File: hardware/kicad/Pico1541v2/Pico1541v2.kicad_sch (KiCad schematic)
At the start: 48 parts, among them J1 SWD, J2 Serial, J3 Display/Keys, J4 Micro SD Card, J5 OLED/Key_Hat, J6 OLED, J7 DIN-6, Q1 MMBT3904, SW1 Reset, SW2 Button1, SW3 Button2, SW4 Button3, SW5 Button4, U1 74LS06, U2 SRV05-4

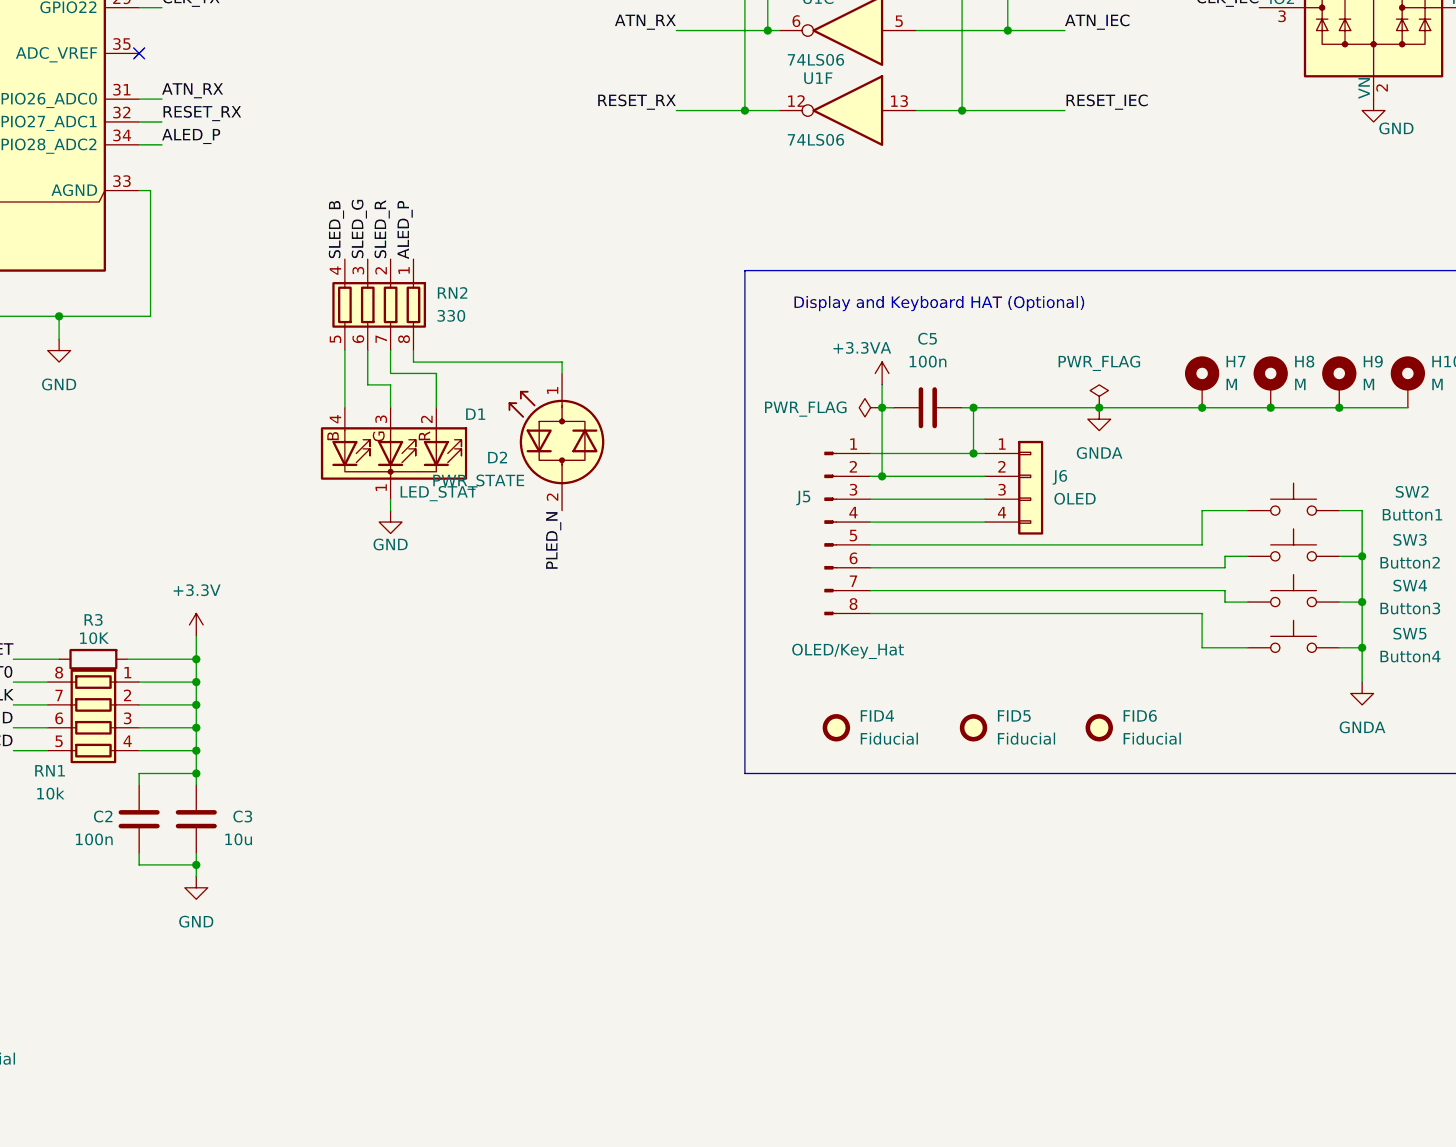
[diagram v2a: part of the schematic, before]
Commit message: Use real-time sampling of ATN signal if the IRQ flag is false. Not fixing the real issue, but seems to not impact performance any significantly.
More updates on the hardware.
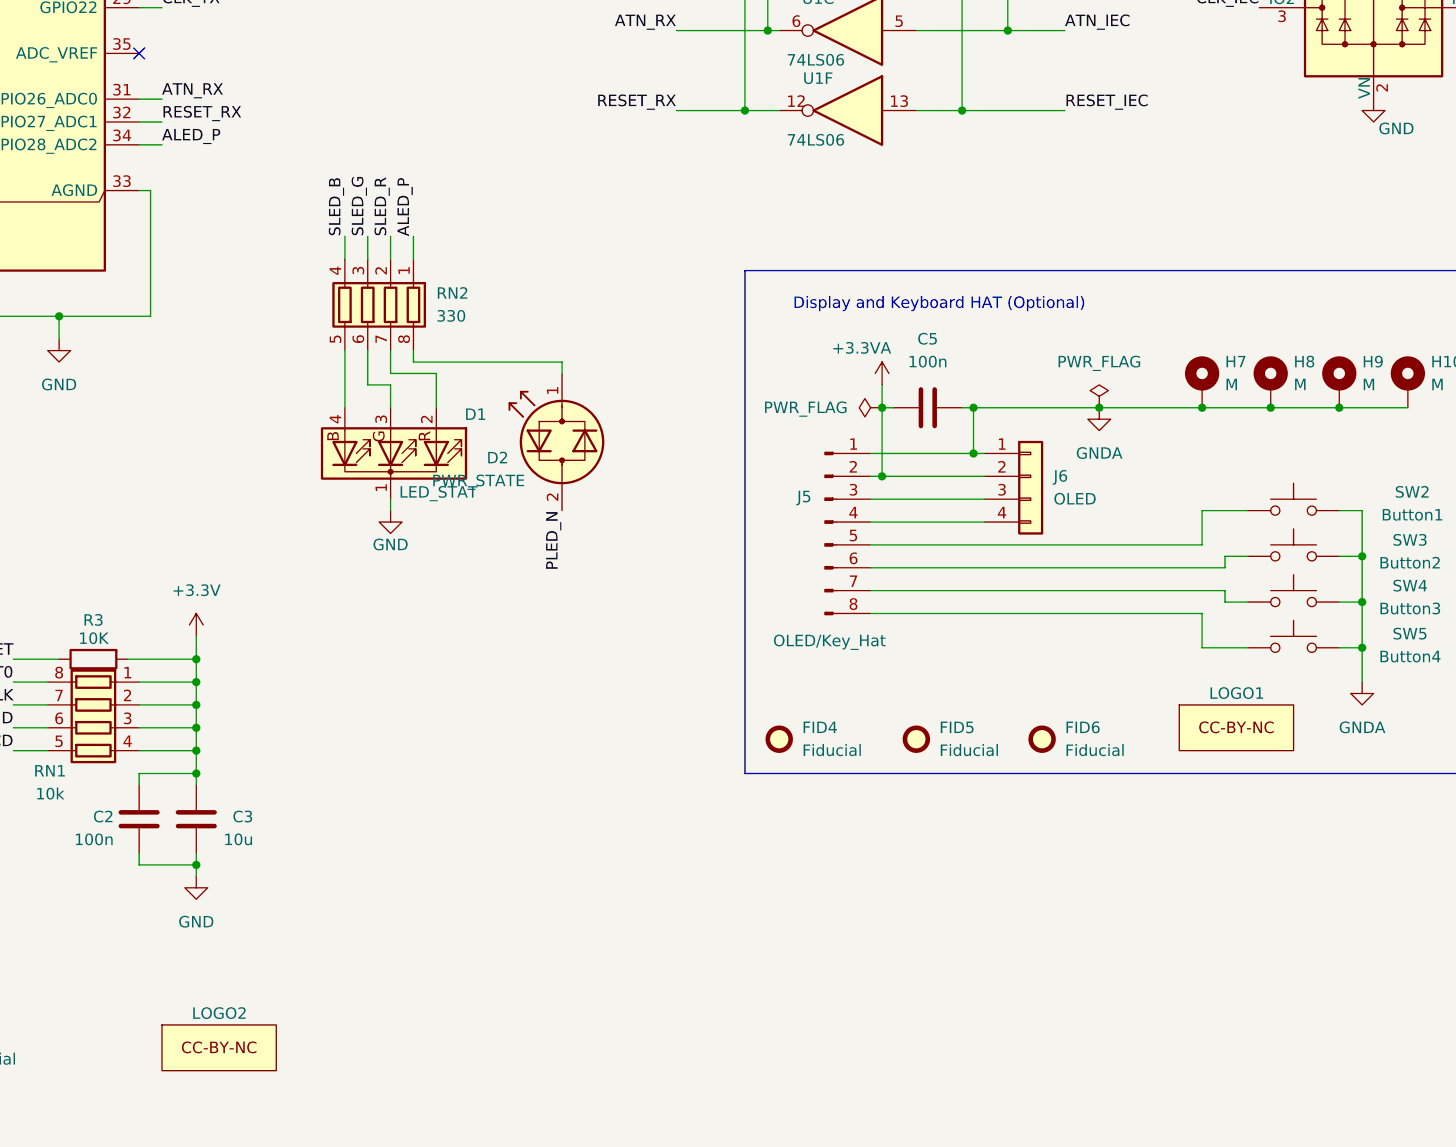
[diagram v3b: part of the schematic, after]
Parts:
- added LOGO1, LOGO2: (no value), Symbol:Symbol_CC-Noncommercial_CopperTop_Small, symbol Pico1541:CC-BY-NC
- SW2, SW3, SW4, SW5: footprint Button_Switch_SMD:SW_SPST_EVPBF -> Button_Switch_SMD:SW_SPST_Omron_B3FS-100xP
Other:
- moved on the sheet: FID4, FID5, FID6
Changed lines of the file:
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@@
 	(wire
 		(pts
+			(xy 151.13 97.79) (xy 151.13 100.33)
+		)
+		(stroke
+			(width 0)
+			(type default)
+		)
+	)
+	(wire
+		(pts
 			(xy 123.19 57.15) (xy 120.65 57.15)
 		)
@@
 	(wire
 		(pts
+			(xy 143.51 97.79) (xy 143.51 100.33)
+		)
+		(stroke
+			(width 0)
+			(type default)
+		)
+	)
+	(wire
+		(pts
 			(xy 146.05 114.3) (xy 148.59 114.3)
 		)
@@
 	(wire
 		(pts
+			(xy 146.05 97.79) (xy 146.05 100.33)
+		)
+		(stroke
+			(width 0)
+			(type default)
+		)
+	)
+	(wire
+		(pts
 			(xy 256.54 143.51) (xy 256.54 147.32)
 		)
@@
 	(wire
 		(pts
+			(xy 148.59 97.79) (xy 148.59 100.33)
+		)
+		(stroke
+			(width 0)
+			(type default)
+		)
+	)
+	(wire
+		(pts
 			(xy 227.33 116.84) (xy 238.76 116.84)
 		)
@@
 	)
 	(label "SLED_R"
-		(at 148.59 100.33 90)
+		(at 148.59 97.79 90)
 		(effects
 			(font
@@
 	)
 	(label "SLED_G"
-		(at 146.05 100.33 90)
+		(at 146.05 97.79 90)
 		(effects
 			(font
@@
 	)
 	(label "ALED_P"
-		(at 151.13 100.33 90)
+		(at 151.13 97.79 90)
 		(effects
 			(font
@@
 	)
 	(label "SLED_B"
-		(at 143.51 100.33 90)
+		(at 143.51 97.79 90)
 		(effects
 			(font
@@
 	)
 	(symbol
+		(lib_id "Pico1541:CC-BY-NC")
+		(at 129.54 187.96 0)
+		(unit 1)
+		(body_style 1)
+		(exclude_from_sim no)
+		(in_bom yes)
+		(on_board yes)
+		(in_pos_files yes)
+		(dnp no)
+		(property "Reference" "LOGO2"
+			(at 126.492 184.15 0)
+			(show_name no)
+			(do_not_autoplace no)
+			(effects
+				(font
+					(size 1.27 1.27)
+				)
+				(justify left)
+			)
+		)
+		(property "Value" ""
+			(at 129.54 187.96 0)
+			(show_name no)
+			(do_not_autoplace no)
+			(effects
+				(font
+					(size 1.27 1.27)
+				)
+			)
+		)
+		(property "Footprint" "Symbol:Symbol_CC-Noncommercial_CopperTop_Small"
+			(at 129.54 187.96 0)
+			(hide yes)
+			(show_name no)
+			(do_not_autoplace no)
+			(effects
+				(font
+					(size 1.27 1.27)
+				)
+			)
+		)
+		(property "Datasheet" ""
+			(at 129.54 187.96 0)
+			(hide yes)
+			(show_name no)
+			(do_not_autoplace no)
+			(effects
+				(font
+					(size 1.27 1.27)
+				)
+			)
+		)
+		(property "Description" ""
+			(at 129.54 187.96 0)
+			(hide yes)
+			(show_name no)
+			(do_not_autoplace no)
+			(effects
+				(font
+					(size 1.27 1.27)
+				)
+			)
+		)
+		(instances
+			(project "Pico1541v2"
+				(path "/fb7a9a9a-73a1-4d45-b1f9-1589f10de67b"
+					(reference "LOGO2")
+					(unit 1)
+				)
+			)
+		)
+	)
+	(symbol
+		(lib_id "Pico1541:CC-BY-NC")
+		(at 242.57 152.4 0)
+		(unit 1)
+		(body_style 1)
+		(exclude_from_sim no)
+		(in_bom yes)
+		(on_board yes)
+		(in_pos_files yes)
+		(dnp no)
+		(property "Reference" "LOGO1"
+			(at 239.522 148.59 0)
+			(show_name no)
+			(do_not_autoplace no)
+			(effects
+				(font
+					(size 1.27 1.27)
+				)
+				(justify left)
+			)
+		)
+		(property "Value" ""
+			(at 242.57 152.4 0)
+			(show_name no)
+			(do_not_autoplace no)
+			(effects
+				(font
+					(size 1.27 1.27)
+				)
+			)
+		)
+		(property "Footprint" "Symbol:Symbol_CC-Noncommercial_CopperTop_Small"
+			(at 242.57 152.4 0)
+			(hide yes)
+			(show_name no)
+			(do_not_autoplace no)
+			(effects
+				(font
+					(size 1.27 1.27)
+				)
+			)
+		)
+		(property "Datasheet" ""
+			(at 242.57 152.4 0)
+			(hide yes)
+			(show_name no)
+			(do_not_autoplace no)
+			(effects
+				(font
+					(size 1.27 1.27)
+				)
+			)
+		)
+		(property "Description" ""
+			(at 242.57 152.4 0)
+			(hide yes)
+			(show_name no)
+			(do_not_autoplace no)
+			(effects
+				(font
+					(size 1.27 1.27)
+				)
+			)
+		)
+		(instances
+			(project "Pico1541v2"
+				(path "/fb7a9a9a-73a1-4d45-b1f9-1589f10de67b"
+					(reference "LOGO1")
+					(unit 1)
+				)
+			)
+		)
+	)
+	(symbol
 		(lib_id "Device:R_Pack04")
 		(at 115.57 152.4 90)
@@
 	(symbol
 		(lib_id "Mechanical:Fiducial")
-		(at 227.33 152.4 0)
+		(at 220.98 153.67 0)
 		(unit 1)
 		(body_style 1)
@@
 		(fields_autoplaced yes)
 		(property "Reference" "FID6"
-			(at 229.87 151.1299 0)
+			(at 223.52 152.3999 0)
 			(show_name no)
 			(do_not_autoplace no)
@@
 		)
 		(property "Value" "Fiducial"
-			(at 229.87 153.6699 0)
+			(at 223.52 154.9399 0)
 			(show_name no)
 			(do_not_autoplace no)
@@
 		)
 		(property "Footprint" "Fiducial:Fiducial_1mm_Mask3mm"
-			(at 227.33 152.4 0)
+			(at 220.98 153.67 0)
 			(hide yes)
 			(show_name no)
@@
 		)
 		(property "Datasheet" ""
-			(at 227.33 152.4 0)
+			(at 220.98 153.67 0)
 			(hide yes)
 			(show_name no)
@@
 		)
 		(property "Description" "Fiducial Marker"
-			(at 227.33 152.4 0)
+			(at 220.98 153.67 0)
 			(hide yes)
 			(show_name no)
@@
 			)
 		)
-		(property "Footprint" "Button_Switch_SMD:SW_SPST_EVPBF"
+		(property "Footprint" "Button_Switch_SMD:SW_SPST_Omron_B3FS-100xP"
 			(at 248.92 133.35 0)
 			(hide yes)
@@
 			)
 		)
-		(property "Footprint" "Button_Switch_SMD:SW_SPST_EVPBF"
+		(property "Footprint" "Button_Switch_SMD:SW_SPST_Omron_B3FS-100xP"
 			(at 248.92 128.27 0)
 			(hide yes)
@@
 	(symbol
 		(lib_id "Mechanical:Fiducial")
-		(at 198.12 152.4 0)
+		(at 191.77 153.67 0)
 		(unit 1)
 		(body_style 1)
@@
 		(fields_autoplaced yes)
 		(property "Reference" "FID4"
-			(at 200.66 151.1299 0)
+			(at 194.31 152.3999 0)
 			(show_name no)
 			(do_not_autoplace no)
@@
 		)
 		(property "Value" "Fiducial"
-			(at 200.66 153.6699 0)
+			(at 194.31 154.9399 0)
 			(show_name no)
 			(do_not_autoplace no)
@@
 		)
 		(property "Footprint" "Fiducial:Fiducial_1mm_Mask3mm"
-			(at 198.12 152.4 0)
+			(at 191.77 153.67 0)
 			(hide yes)
 			(show_name no)
@@
 		)
 		(property "Datasheet" ""
-			(at 198.12 152.4 0)
+			(at 191.77 153.67 0)
 			(hide yes)
 			(show_name no)
@@
 		)
 		(property "Description" "Fiducial Marker"
-			(at 198.12 152.4 0)
+			(at 191.77 153.67 0)
 			(hide yes)
 			(show_name no)
@@
 			)
 		)
-		(property "Footprint" "Button_Switch_SMD:SW_SPST_EVPBF"
+		(property "Footprint" "Button_Switch_SMD:SW_SPST_Omron_B3FS-100xP"
 			(at 248.92 138.43 0)
 			(hide yes)
@@
 		)
 		(property "Value" "OLED/Key_Hat"
-			(at 199.39 143.764 0)
+			(at 197.358 142.748 0)
 			(show_name no)
 			(do_not_autoplace no)
@@
 			)
 		)
-		(property "Footprint" "Button_Switch_SMD:SW_SPST_EVPBF"
+		(property "Footprint" "Button_Switch_SMD:SW_SPST_Omron_B3FS-100xP"
 			(at 248.92 123.19 0)
 			(hide yes)
@@
 	(symbol
 		(lib_id "Mechanical:Fiducial")
-		(at 213.36 152.4 0)
+		(at 207.01 153.67 0)
 		(unit 1)
 		(body_style 1)
@@
 		(fields_autoplaced yes)
 		(property "Reference" "FID5"
-			(at 215.9 151.1299 0)
+			(at 209.55 152.3999 0)
 			(show_name no)
 			(do_not_autoplace no)
@@
 		)
 		(property "Value" "Fiducial"
-			(at 215.9 153.6699 0)
+			(at 209.55 154.9399 0)
 			(show_name no)
 			(do_not_autoplace no)
@@
 		)
 		(property "Footprint" "Fiducial:Fiducial_1mm_Mask3mm"
-			(at 213.36 152.4 0)
+			(at 207.01 153.67 0)
 			(hide yes)
 			(show_name no)
@@
 		)
 		(property "Datasheet" ""
-			(at 213.36 152.4 0)
+			(at 207.01 153.67 0)
 			(hide yes)
 			(show_name no)
@@
 		)
 		(property "Description" "Fiducial Marker"
-			(at 213.36 152.4 0)
+			(at 207.01 153.67 0)
 			(hide yes)
 			(show_name no)

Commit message: Updated V2 hardware.
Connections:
- net PLED_N is gone; now on net ALED_N: D2.2 (AK)
- net ALED_P: now also A1.14 (GPIO10); no longer A1.34 (GPIO28_ADC2)
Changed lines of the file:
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@@
-	)
-	(no_connect
-		(at 74.93 80.01)
 	)
 	(no_connect
@@
 	)
 	(no_connect
+		(at 120.65 87.63)
+	)
+	(no_connect
 		(at 74.93 49.53)
 	)
@@
 	(wire
 		(pts
+			(xy 71.12 80.01) (xy 74.93 80.01)
+		)
+		(stroke
+			(width 0)
+			(type default)
+		)
+	)
+	(wire
+		(pts
 			(xy 241.3 138.43) (xy 241.3 137.16)
 		)
@@
 		(pts
 			(xy 204.47 116.84) (xy 203.2 116.84)
-		)
-		(stroke
-			(width 0)
-			(type default)
-		)
-	)
-	(wire
-		(pts
-			(xy 123.19 87.63) (xy 120.65 87.63)
 		)
 		(stroke
@@
 		)
 	)
-	(label "PLED_N"
+	(label "ALED_N"
 		(at 167.64 128.27 270)
 		(effects
@@
 	)
 	(label "ALED_P"
-		(at 123.19 87.63 0)
-		(effects
-			(font
-				(size 1.27 1.27)
-			)
-			(justify left bottom)
-		)
-	)
+		(at 71.12 80.01 180)
+		(effects
+			(font
+				(size 1.27 1.27)
+			)
+			(justify right bottom)
+		)
+	)

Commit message: More hardware updates.
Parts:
- removed H6: M, MountingHole:MountingHole_2.5mm_Pad_Via, symbol Mechanical:MountingHole_Pad
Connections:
- net ATN_IEC: now also RN4.6 (R3.2), U1.1; no longer RN4.7 (R2.2), U1.5
- net ATN_RX: now also RN3.7 (R2.2), U1.2; no longer RN3.8 (R1.2), U1.6
- net CLK_IEC: now also RN4.7 (R2.2), U1.10, U1.3; no longer RN4.6 (R3.2), U1.11, U1.2
- net CLK_RX: now also RN3.8 (R1.2), U1.4; no longer RN3.6 (R3.2), U1.10
- net CLK_TX: now also U1.11; no longer U1.1
- net DATA_IEC: now also U1.6; no longer U1.4
- net DATA_TX: now also U1.5; no longer U1.3
- net RESET_RX: now also RN3.6 (R3.2); no longer RN3.7 (R2.2)
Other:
- moved on the sheet: U1A, U1B, U1C, U1E

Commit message: Added symbol library which contains the CC logo. Added new mousebites footprint
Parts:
- removed LOGO1, LOGO2: (no value), Symbol:Symbol_CC-Noncommercial_CopperTop_Small, symbol Pico1541:CC-BY-NC
- added CC1, CC2: (no value), Symbol:Symbol_CC-Noncommercial_CopperTop_Small, symbol Pico1541:CC-BY-NC
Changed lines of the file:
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@@
 	)
 	(symbol
-		(lib_id "Pico1541:CC-BY-NC")
-		(at 129.54 187.96 0)
-		(unit 1)
-		(body_style 1)
-		(exclude_from_sim no)
-		(in_bom yes)
-		(on_board yes)
-		(in_pos_files yes)
-		(dnp no)
-		(property "Reference" "LOGO2"
-			(at 126.492 184.15 0)
-			(show_name no)
-			(do_not_autoplace no)
-			(effects
-				(font
-					(size 1.27 1.27)
-				)
-				(justify left)
-			)
-		)
-		(property "Value" ""
-			(at 129.54 187.96 0)
-			(show_name no)
-			(do_not_autoplace no)
-			(effects
-				(font
-					(size 1.27 1.27)
-				)
-			)
-		)
-		(property "Footprint" "Symbol:Symbol_CC-Noncommercial_CopperTop_Small"
-			(at 129.54 187.96 0)
-			(hide yes)
-			(show_name no)
-			(do_not_autoplace no)
-			(effects
-				(font
-					(size 1.27 1.27)
-				)
-			)
-		)
-		(property "Datasheet" ""
-			(at 129.54 187.96 0)
-			(hide yes)
-			(show_name no)
-			(do_not_autoplace no)
-			(effects
-				(font
-					(size 1.27 1.27)
-				)
-			)
-		)
-		(property "Description" ""
-			(at 129.54 187.96 0)
-			(hide yes)
-			(show_name no)
-			(do_not_autoplace no)
-			(effects
-				(font
-					(size 1.27 1.27)
-				)
-			)
-		)
-		(instances
-			(project "Pico1541v2"
-				(path "/fb7a9a9a-73a1-4d45-b1f9-1589f10de67b"
-					(reference "LOGO2")
-					(unit 1)
-				)
-			)
-		)
-	)
-	(symbol
-		(lib_id "Pico1541:CC-BY-NC")
-		(at 242.57 152.4 0)
-		(unit 1)
-		(body_style 1)
-		(exclude_from_sim no)
-		(in_bom yes)
-		(on_board yes)
-		(in_pos_files yes)
-		(dnp no)
-		(property "Reference" "LOGO1"
-			(at 239.522 148.59 0)
-			(show_name no)
-			(do_not_autoplace no)
-			(effects
-				(font
-					(size 1.27 1.27)
-				)
-				(justify left)
-			)
-		)
-		(property "Value" ""
-			(at 242.57 152.4 0)
-			(show_name no)
-			(do_not_autoplace no)
-			(effects
-				(font
-					(size 1.27 1.27)
-				)
-			)
-		)
-		(property "Footprint" "Symbol:Symbol_CC-Noncommercial_CopperTop_Small"
-			(at 242.57 152.4 0)
-			(hide yes)
-			(show_name no)
-			(do_not_autoplace no)
-			(effects
-				(font
-					(size 1.27 1.27)
-				)
-			)
-		)
-		(property "Datasheet" ""
-			(at 242.57 152.4 0)
-			(hide yes)
-			(show_name no)
-			(do_not_autoplace no)
-			(effects
-				(font
-					(size 1.27 1.27)
-				)
-			)
-		)
-		(property "Description" ""
-			(at 242.57 152.4 0)
-			(hide yes)
-			(show_name no)
-			(do_not_autoplace no)
-			(effects
-				(font
-					(size 1.27 1.27)
-				)
-			)
-		)
-		(instances
-			(project "Pico1541v2"
-				(path "/fb7a9a9a-73a1-4d45-b1f9-1589f10de67b"
-					(reference "LOGO1")
-					(unit 1)
-				)
-			)
-		)
-	)
-	(symbol
 		(lib_id "Device:R_Pack04")
 		(at 115.57 152.4 90)
@@
 	)
 	(symbol
+		(lib_id "Pico1541:CC-BY-NC")
+		(at 128.27 187.96 0)
+		(unit 1)
+		(body_style 1)
+		(exclude_from_sim no)
+		(in_bom yes)
+		(on_board yes)
+		(in_pos_files yes)
+		(dnp no)
+		(fields_autoplaced yes)
+		(property "Reference" "CC1"
+			(at 135.89 187.9599 0)
+			(show_name no)
+			(do_not_autoplace no)
+			(effects
+				(font
+					(size 1.27 1.27)
+				)
+				(justify left)
+			)
+		)
+		(property "Value" ""
+			(at 128.27 187.96 0)
+			(show_name no)
+			(do_not_autoplace no)
+			(effects
+				(font
+					(size 1.27 1.27)
+				)
+			)
+		)
+		(property "Footprint" "Symbol:Symbol_CC-Noncommercial_CopperTop_Small"
+			(at 128.016 191.516 0)
+			(hide yes)
+			(show_name no)
+			(do_not_autoplace no)
+			(effects
+				(font
+					(size 1.27 1.27)
+				)
+			)
+		)
+		(property "Datasheet" ""
+			(at 128.27 187.96 0)
+			(hide yes)
+			(show_name no)
+			(do_not_autoplace no)
+			(effects
+				(font
+					(size 1.27 1.27)
+				)
+			)
+		)
+		(property "Description" ""
+			(at 128.27 187.96 0)
+			(hide yes)
+			(show_name no)
+			(do_not_autoplace no)
+			(effects
+				(font
+					(size 1.27 1.27)
+				)
+			)
+		)
+		(instances
+			(project "Pico1541v2"
+				(path "/fb7a9a9a-73a1-4d45-b1f9-1589f10de67b"
+					(reference "CC1")
+					(unit 1)
+				)
+			)
+		)
+	)
+	(symbol
 		(lib_id "power:GND")
 		(at 73.66 151.13 90)
@@
 					(unit 1)
 				)
+			)
+		)
+	)
+	(symbol
+		(lib_id "Pico1541:CC-BY-NC")
+		(at 240.03 153.67 0)
+		(unit 1)
+		(body_style 1)
+		(exclude_from_sim no)
+		(in_bom yes)
+		(on_board yes)
+		(in_pos_files yes)
+		(dnp no)
+		(fields_autoplaced yes)
+		(property "Reference" "CC2"
+			(at 247.65 153.6699 0)
+			(show_name no)
+			(do_not_autoplace no)
+			(effects
+				(font
+					(size 1.27 1.27)
+				)
+				(justify left)
+			)
+		)
+		(property "Value" ""
+			(at 240.03 153.67 0)
+			(show_name no)
+			(do_not_autoplace no)
+			(effects
+				(font
+					(size 1.27 1.27)
+				)
+			)
+		)
+		(property "Footprint" "Symbol:Symbol_CC-Noncommercial_CopperTop_Small"
+			(at 239.776 157.226 0)
+			(hide yes)
+			(show_name no)
+			(do_not_autoplace no)
+			(effects
+				(font
+					(size 1.27 1.27)
+				)
+			)
+		)
+		(property "Datasheet" ""
+			(at 240.03 153.67 0)
+			(hide yes)
+			(show_name no)
+			(do_not_autoplace no)
+			(effects
+				(font
+					(size 1.27 1.27)
+				)
+			)
+		)
+		(property "Description" ""
+			(at 240.03 153.67 0)
+			(hide yes)
+			(show_name no)
+			(do_not_autoplace no)
+			(effects
+				(font
+					(size 1.27 1.27)
+				)
+			)
+		)
+		(instances
+			(project "Pico1541v2"
+				(path "/fb7a9a9a-73a1-4d45-b1f9-1589f10de67b"
+					(reference "CC2")
+					(unit 1)
+				)
